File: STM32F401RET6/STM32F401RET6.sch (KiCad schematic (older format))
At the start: 12 parts, among them U7 STM32F401RETx

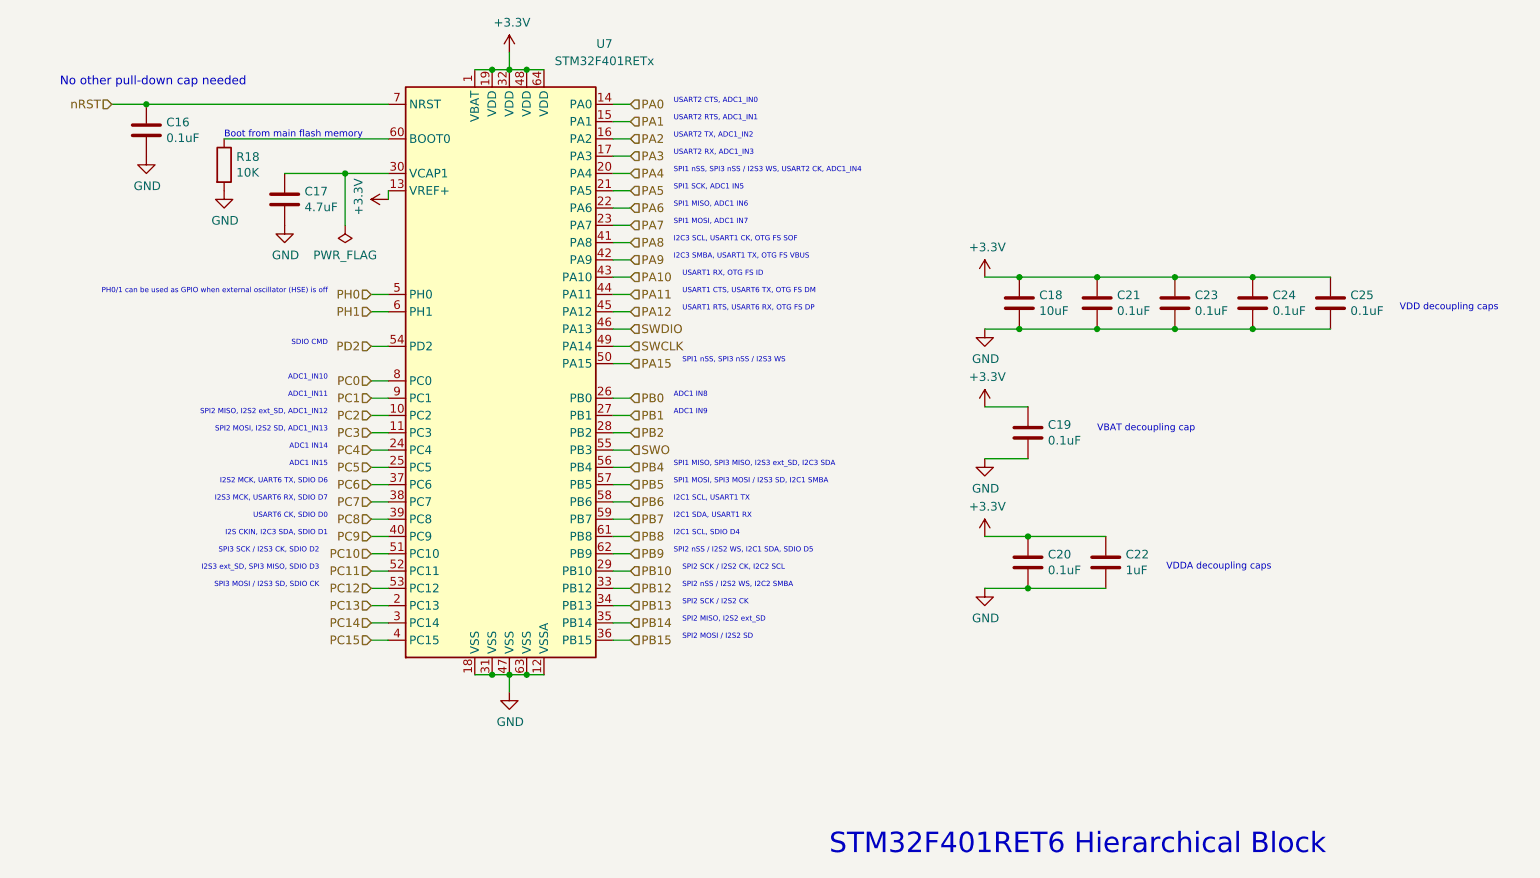
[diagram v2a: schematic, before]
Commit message: Revert schematics so that it can merge
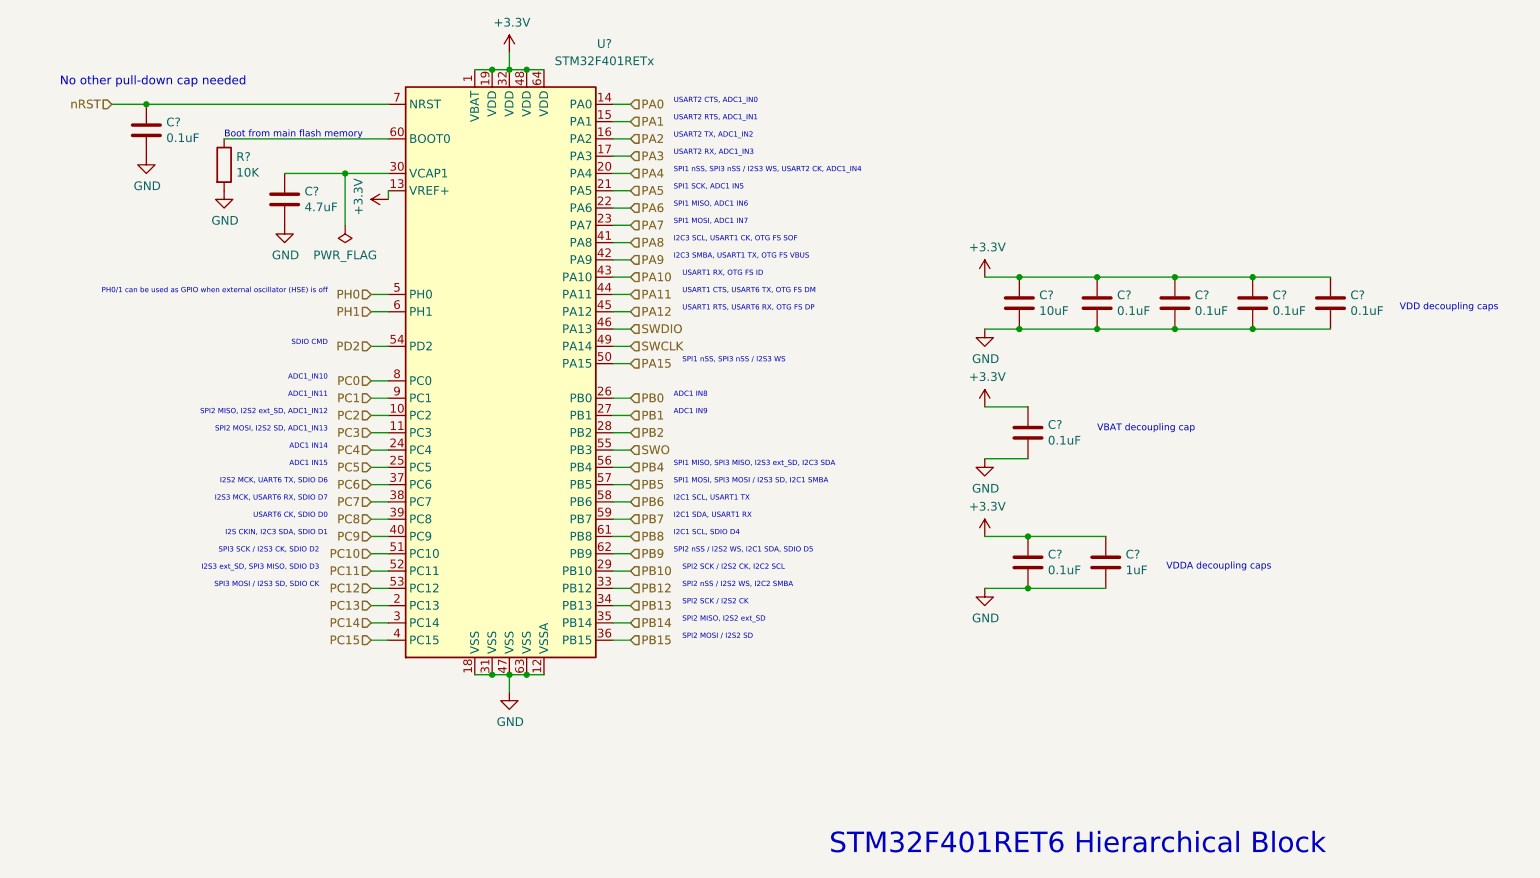
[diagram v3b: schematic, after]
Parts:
- renumbered C22 to C?, C18 to C?, C21 to C?, C23 to C?, C24 to C?, C25 to C?, C17 to C?, C16 to C?, C19 to C?, C20 to C?, R18 to R?, U7 to U?
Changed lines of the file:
@@
 $Descr A4 11693 8268
 encoding utf-8
-Sheet 6 6
+Sheet 4 6
 Title ""
 Date ""
@@
 $EndDescr
 $Comp
-L MCU_ST_STM32F4:STM32F401RETx U7
+L MCU_ST_STM32F4:STM32F401RETx U?
 U 1 1 5DE1731E
 P 5250 4100
-F 0 "U7" H 5800 5950 50  0000 C CNN
+F 0 "U?" H 5800 5950 50  0000 C CNN
 F 1 "STM32F401RETx" H 5800 5850 50  0000 C CNN
 F 2 "Package_QFP:LQFP-64_10x10mm_P0.5mm" H 4650 2400 50  0001 R CNN
@@
 	5250 2300 5250 2400
 $Comp
-L power:GND #PWR093
+L power:GND #PWR?
 U 1 1 5DE18883
 P 5250 6000
-F 0 "#PWR093" H 5250 5750 50  0001 C CNN
+F 0 "#PWR?" H 5250 5750 50  0001 C CNN
 F 1 "GND" H 5255 5827 50  0000 C CNN
 F 2 "" H 5250 6000 50  0001 C CNN
@@
 	5250 6000 5250 5900
 $Comp
-L Device:C C21
+L Device:C C?
 U 1 1 5DE19367
 P 8650 3750
-F 0 "C21" H 8765 3796 50  0000 L CNN
+F 0 "C?" H 8765 3796 50  0000 L CNN
 F 1 "0.1uF" H 8765 3705 50  0000 L CNN
 F 2 "" H 8688 3600 50  0001 C CNN
@@
 $EndComp
 $Comp
-L Device:C C23
+L Device:C C?
 U 1 1 5DE19787
 P 9100 3750
-F 0 "C23" H 9215 3796 50  0000 L CNN
+F 0 "C?" H 9215 3796 50  0000 L CNN
 F 1 "0.1uF" H 9215 3705 50  0000 L CNN
 F 2 "" H 9138 3600 50  0001 C CNN
@@
 $EndComp
 $Comp
-L Device:C C24
+L Device:C C?
 U 1 1 5DE19D37
 P 9550 3750
-F 0 "C24" H 9665 3796 50  0000 L CNN
+F 0 "C?" H 9665 3796 50  0000 L CNN
 F 1 "0.1uF" H 9665 3705 50  0000 L CNN
 F 2 "" H 9588 3600 50  0001 C CNN
@@
 $EndComp
 $Comp
-L Device:C C25
+L Device:C C?
 U 1 1 5DE19F0D
 P 10000 3750
-F 0 "C25" H 10115 3796 50  0000 L CNN
+F 0 "C?" H 10115 3796 50  0000 L CNN
 F 1 "0.1uF" H 10115 3705 50  0000 L CNN
 F 2 "" H 10038 3600 50  0001 C CNN
@@
 	8200 3900 8650 3900
 $Comp
-L Device:C C18
+L Device:C C?
 U 1 1 5DE19136
 P 8200 3750
-F 0 "C18" H 8315 3796 50  0000 L CNN
+F 0 "C?" H 8315 3796 50  0000 L CNN
 F 1 "10uF" H 8315 3705 50  0000 L CNN
 F 2 "" H 8238 3600 50  0001 C CNN
@@
 $EndComp
 $Comp
-L power:GND #PWR095
+L power:GND #PWR?
 U 1 1 5DE18B06
 P 8000 3900
-F 0 "#PWR095" H 8000 3650 50  0001 C CNN
+F 0 "#PWR?" H 8000 3650 50  0001 C CNN
 F 1 "GND" H 8005 3727 50  0000 C CNN
 F 2 "" H 8000 3900 50  0001 C CNN
@@
 $EndComp
 $Comp
-L power:GND #PWR097
+L power:GND #PWR?
 U 1 1 5DE1D921
 P 8000 4650
-F 0 "#PWR097" H 8000 4400 50  0001 C CNN
+F 0 "#PWR?" H 8000 4400 50  0001 C CNN
 F 1 "GND" H 8005 4477 50  0000 C CNN
 F 2 "" H 8000 4650 50  0001 C CNN
@@
 $EndComp
 $Comp
-L Device:C C19
+L Device:C C?
 U 1 1 5DE1DB7A
 P 8250 4500
-F 0 "C19" H 8365 4546 50  0000 L CNN
+F 0 "C?" H 8365 4546 50  0000 L CNN
 F 1 "0.1uF" H 8365 4455 50  0000 L CNN
 F 2 "" H 8288 4350 50  0001 C CNN
@@
 	8250 4350 8000 4350
 $Comp
-L Device:C C20
+L Device:C C?
 U 1 1 5DE1EBB5
 P 8250 5250
-F 0 "C20" H 8365 5296 50  0000 L CNN
+F 0 "C?" H 8365 5296 50  0000 L CNN
 F 1 "0.1uF" H 8365 5205 50  0000 L CNN
 F 2 "" H 8288 5100 50  0001 C CNN
@@
 $EndComp
 $Comp
-L power:GND #PWR099
+L power:GND #PWR?
 U 1 1 5DE1F4FA
 P 8000 5400
-F 0 "#PWR099" H 8000 5150 50  0001 C CNN
+F 0 "#PWR?" H 8000 5150 50  0001 C CNN
 F 1 "GND" H 8005 5227 50  0000 C CNN
 F 2 "" H 8000 5400 50  0001 C CNN
@@
 $EndComp
 $Comp
-L Device:C C22
+L Device:C C?
 U 1 1 5DE17F46
 P 8700 5250
-F 0 "C22" H 8815 5296 50  0000 L CNN
+F 0 "C?" H 8815 5296 50  0000 L CNN
 F 1 "1uF" H 8815 5205 50  0000 L CNN
 F 2 "" H 8738 5100 50  0001 C CNN
@@
 VDD decoupling caps
 $Comp
-L Device:C C17
+L Device:C C?
 U 1 1 5DE1ABC6
 P 3950 3150
-F 0 "C17" H 4065 3196 50  0000 L CNN
+F 0 "C?" H 4065 3196 50  0000 L CNN
 F 1 "4.7uF" H 4065 3105 50  0000 L CNN
 F 2 "" H 3988 3000 50  0001 C CNN
@@
 $EndComp
 $Comp
-L power:GND #PWR090
+L power:GND #PWR?
 U 1 1 5DE1B283
 P 3950 3300
-F 0 "#PWR090" H 3950 3050 50  0001 C CNN
+F 0 "#PWR?" H 3950 3050 50  0001 C CNN
 F 1 "GND" H 3955 3127 50  0000 C CNN
 F 2 "" H 3950 3300 50  0001 C CNN
@@
 	3950 3000 4300 3000
 $Comp
-L Device:C C16
+L Device:C C?
 U 1 1 5DE1BE22
 P 3150 2750
-F 0 "C16" H 3265 2796 50  0000 L CNN
+F 0 "C?" H 3265 2796 50  0000 L CNN
 F 1 "0.1uF" H 3265 2705 50  0000 L CNN
 F 2 "" H 3188 2600 50  0001 C CNN
@@
 	2950 2600 3150 2600
 $Comp
-L power:GND #PWR088
+L power:GND #PWR?
 U 1 1 5DE1D367
 P 3150 2900
-F 0 "#PWR088" H 3150 2650 50  0001 C CNN
+F 0 "#PWR?" H 3150 2650 50  0001 C CNN
 F 1 "GND" H 3155 2727 50  0000 C CNN
 F 2 "" H 3150 2900 50  0001 C CNN
@@
 Connection ~ 3150 2600
 $Comp
-L Device:R R18
+L Device:R R?
 U 1 1 5DE1E2D2
 P 3600 2950
-F 0 "R18" H 3670 2996 50  0000 L CNN
+F 0 "R?" H 3670 2996 50  0000 L CNN
 F 1 "10K" H 3670 2905 50  0000 L CNN
 F 2 "" V 3530 2950 50  0001 C CNN
@@
 $EndComp
 $Comp
-L power:GND #PWR089
+L power:GND #PWR?
 U 1 1 5DE1E857
 P 3600 3100
-F 0 "#PWR089" H 3600 2850 50  0001 C CNN
+F 0 "#PWR?" H 3600 2850 50  0001 C CNN
 F 1 "GND" H 3605 2927 50  0000 C CNN
 F 2 "" H 3600 3100 50  0001 C CNN
@@
 SPI2 nSS / I2S2 WS, I2C1 SDA, SDIO D5
 $Comp
-L power:+3.3V #PWR092
+L power:+3.3V #PWR?
 U 1 1 5DE1F0DC
 P 5250 2300
-F 0 "#PWR092" H 5250 2150 50  0001 C CNN
+F 0 "#PWR?" H 5250 2150 50  0001 C CNN
 F 1 "+3.3V" H 5265 2473 50  0000 C CNN
 F 2 "" H 5250 2300 50  0001 C CNN
@@
 $EndComp
 $Comp
-L power:+3.3V #PWR094
+L power:+3.3V #PWR?
 U 1 1 5DE22E45
 P 8000 3600
-F 0 "#PWR094" H 8000 3450 50  0001 C CNN
+F 0 "#PWR?" H 8000 3450 50  0001 C CNN
 F 1 "+3.3V" H 8015 3773 50  0000 C CNN
 F 2 "" H 8000 3600 50  0001 C CNN
@@
 $EndComp
 $Comp
-L power:+3.3V #PWR096
+L power:+3.3V #PWR?
 U 1 1 5DE235AC
 P 8000 4350
-F 0 "#PWR096" H 8000 4200 50  0001 C CNN
+F 0 "#PWR?" H 8000 4200 50  0001 C CNN
 F 1 "+3.3V" H 8015 4523 50  0000 C CNN
 F 2 "" H 8000 4350 50  0001 C CNN
@@
 $EndComp
 $Comp
-L power:+3.3V #PWR098
+L power:+3.3V #PWR?
 U 1 1 5DE2397A
 P 8000 5100
-F 0 "#PWR098" H 8000 4950 50  0001 C CNN
+F 0 "#PWR?" H 8000 4950 50  0001 C CNN
 F 1 "+3.3V" H 8015 5273 50  0000 C CNN
 F 2 "" H 8000 5100 50  0001 C CNN
@@
 STM32F401RET6 Hierarchical Block
 $Comp
-L power:+3.3V #PWR091
+L power:+3.3V #PWR?
 U 1 1 5DE2F79B
 P 4550 3150
-F 0 "#PWR091" H 4550 3000 50  0001 C CNN
+F 0 "#PWR?" H 4550 3000 50  0001 C CNN
 F 1 "+3.3V" H 4565 3323 50  0000 C CNN
 F 2 "" H 4550 3150 50  0001 C CNN
@@
 	4550 3100 4550 3150
 $Comp
-L power:PWR_FLAG #FLG05
+L power:PWR_FLAG #FLG?
 U 1 1 5DE3436C
 P 4300 3300
-F 0 "#FLG05" H 4300 3375 50  0001 C CNN
+F 0 "#FLG?" H 4300 3375 50  0001 C CNN
 F 1 "PWR_FLAG" H 4300 3473 50  0000 C CNN
 F 2 "" H 4300 3300 50  0001 C CNN
